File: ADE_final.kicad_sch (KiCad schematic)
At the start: 21 parts, among them J7 Conn_01x02_Pin, U8 ADE7953xCP, U9 MCP1825ST-3302E/EB, Y2 3.58M

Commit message: 2nd ADE
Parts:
- added C47, C48: 20p, Capacitor_SMD:C_0603_1608Metric, symbol Device:C
- added C49, C50, C53: 4.7u, Capacitor_SMD:C_0805_2012Metric, symbol Device:C
- added C51, C52, C54: 100n, Capacitor_SMD:C_0603_1608Metric, symbol Device:C
- added R44, R45: 10k, symbol Device:R
- added U10: ADE7953xCP, Package_CSP:LFCSP-28-1EP_5x5mm_P0.5mm_EP3.14x3.14mm, symbol Sensor:ADE7953xCP
- added Y3: 3.58M, Crystal:Crystal_SMD_HC49-SD, symbol Device:Crystal
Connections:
- net +3.3V: now also R44.2, R45.2, U10.17 (VDD), U10.7 (PULL_HIGH), U10.8 (PULL_HIGH)
- net CF1: now also U10.23 (CF1)
- net CF2: now also U10.24 (CF2)
- net GND: now also C47.2, C48.1, C49.1, C50.1, C51.1, C52.1, C53.1, C54.1, R44.1, R45.1, U10.14 (PULL_LOW), U10.16 (AGND), U10.22 (~{IRQ}), U10.28 (~{CS}), U10.29 (EP), U10.4 (DGND)
- net IBN: now also U10.10 (IBN)
- net IBP: now also U10.9 (IBP)
- net MISO: now also U10.26 (MISO/SDA/TX)
- net MOSI: now also U10.27 (MOSI/SCL/RX)
- net RESET: now also U10.2 (~{RESET})
- net REVP: now also U10.20 (~{REVP})
- net SCLK: now also U10.25 (SCLK)
- net ZX_I: now also U10.21 (ZX_I)
- net CLKIN renamed CLKIN1
- net CLKOUT renamed CLKOUT1
- net IAN renamed IAN1
- net IAP renamed IAP1
- net REF renamed REF1
- net VINTA renamed VINTA1
- net VINTD renamed VINTD1
- net VN renamed VN1
- net VP renamed VP1
- net ZX renamed ZX1
- new net CLKIN2: C47.1, U10.18 (CLKIN), Y3.1
- new net CLKOUT2: C48.2, U10.19 (CLKOUT), Y3.2
- new net IAN2: U10.6 (IAN)
- new net IAP2: U10.5 (IAP)
- new net REF2: C53.2, C54.2, U10.13 (REF)
- new net VINTA2: C50.2, C52.2, U10.15 (VINTA)
- new net VINTD2: C49.2, C51.2, U10.3 (VINTD)
- new net VN2: U10.11 (VN)
- new net VP2: U10.12 (VP)
- new net ZX2: U10.1 (ZX)
- no-connect marks 0 -> 6
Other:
- note added: "ADE CH2"
- moved on the sheet: C35, C36, C37, C38, U9, Y2

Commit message: NEW 1A LDO
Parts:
- removed U9: MCP1825ST-3302E/EB, SmartSupplyLib:DDPAK3_MC_MCH, symbol SmartSupplyLib:MCP1825ST-3302E_EB
- added IC3: MIC39100-3.3WS, SOT230P700X180-4N, symbol SamacSys_Parts:MIC39100-3.3WS
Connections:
- net +3.3V: now also IC3.3 (OUT)
- net +5V: now also IC3.1 (IN)
- net GND: now also IC3.2 (GND_1), IC3.4 (GND_2)
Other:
- moved on the sheet: C37, C38

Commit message: CHANGED RELAYS AND CONNECTORS
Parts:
- removed C37: 4.7u, Capacitor_SMD:C_0805_2012Metric, symbol Device:C
- removed C38: 10u, Capacitor_SMD:C_0805_2012Metric, symbol Device:C
- removed IC3: MIC39100-3.3WS, SOT230P700X180-4N, symbol SamacSys_Parts:MIC39100-3.3WS
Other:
- note removed: "Linear voltage regulator"

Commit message: added SD and minor fixes
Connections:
- net IBN is gone; now on net GND: U10.10 (IBN), U8.10 (IBN)
- net IBP is gone; now on net GND: U10.9 (IBP), U8.9 (IBP)
- net GND: no longer R24.1, R25.1, R44.1, R45.1, U10.22 (~{IRQ}), U10.28 (~{CS}), U8.22 (~{IRQ}), U8.28 (~{CS})
- new net CS1: R25.1, U8.28 (~{CS})
- new net CS2: R45.1, U10.28 (~{CS})
- new net IRQ1: R24.1, U8.22 (~{IRQ})
- new net IRQ2: R44.1, U10.22 (~{IRQ})
- no-connect marks 6 -> 4

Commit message: Footprint assignment
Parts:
- C30, C31, C33, C34, C35, C36, C47, C48, C51, C52, C54: footprint Capacitor_SMD:C_0603_1608Metric -> Capacitor_SMD:C_0805_2012Metric
- R24, R25, R44, R45: footprint (none) -> Resistor_SMD:R_0805_2012Metric
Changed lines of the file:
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@@
 			)
 		)
-		(property "Footprint" "Capacitor_SMD:C_0603_1608Metric"
+		(property "Footprint" "Capacitor_SMD:C_0805_2012Metric"
 			(at 132.08 33.3248 0)
 			(hide yes)
@@
 			)
 		)
-		(property "Footprint" ""
+		(property "Footprint" "Resistor_SMD:R_0805_2012Metric"
 			(at 100.838 111.76 90)
 			(hide yes)
@@
 			)
 		)
-		(property "Footprint" ""
+		(property "Footprint" "Resistor_SMD:R_0805_2012Metric"
 			(at 76.708 111.76 90)
 			(hide yes)
@@
 			)
 		)
-		(property "Footprint" "Capacitor_SMD:C_0603_1608Metric"
+		(property "Footprint" "Capacitor_SMD:C_0805_2012Metric"
 			(at 77.7748 16.51 0)
 			(hide yes)
@@
 			)
 		)
-		(property "Footprint" ""
+		(property "Footprint" "Resistor_SMD:R_0805_2012Metric"
 			(at 86.868 111.76 90)
 			(hide yes)
@@
 			)
 		)
-		(property "Footprint" "Capacitor_SMD:C_0603_1608Metric"
+		(property "Footprint" "Capacitor_SMD:C_0805_2012Metric"
 			(at 132.08 16.8148 0)
 			(hide yes)
@@
 			)
 		)
-		(property "Footprint" "Capacitor_SMD:C_0603_1608Metric"
+		(property "Footprint" "Capacitor_SMD:C_0805_2012Metric"
 			(at 32.0548 33.02 0)
 			(hide yes)
@@
 			)
 		)
-		(property "Footprint" "Capacitor_SMD:C_0603_1608Metric"
+		(property "Footprint" "Capacitor_SMD:C_0805_2012Metric"
 			(at 124.46 24.4348 0)
 			(hide yes)
@@
 			)
 		)
-		(property "Footprint" "Capacitor_SMD:C_0603_1608Metric"
+		(property "Footprint" "Capacitor_SMD:C_0805_2012Metric"
 			(at 100.6348 16.51 0)
 			(hide yes)
@@
 			)
 		)
-		(property "Footprint" ""
+		(property "Footprint" "Resistor_SMD:R_0805_2012Metric"
 			(at 110.998 111.76 90)
 			(hide yes)
@@
 			)
 		)
-		(property "Footprint" "Capacitor_SMD:C_0603_1608Metric"
+		(property "Footprint" "Capacitor_SMD:C_0805_2012Metric"
 			(at 77.7748 33.02 0)
 			(hide yes)
@@
 			)
 		)
-		(property "Footprint" "Capacitor_SMD:C_0603_1608Metric"
+		(property "Footprint" "Capacitor_SMD:C_0805_2012Metric"
 			(at 79.7052 91.44 0)
 			(hide yes)
@@
 			)
 		)
-		(property "Footprint" "Capacitor_SMD:C_0603_1608Metric"
+		(property "Footprint" "Capacitor_SMD:C_0805_2012Metric"
 			(at 124.46 40.9448 0)
 			(hide yes)
@@
 			)
 		)
-		(property "Footprint" "Capacitor_SMD:C_0603_1608Metric"
+		(property "Footprint" "Capacitor_SMD:C_0805_2012Metric"
 			(at 32.0548 16.51 0)
 			(hide yes)
@@
 			)
 		)
-		(property "Footprint" "Capacitor_SMD:C_0603_1608Metric"
+		(property "Footprint" "Capacitor_SMD:C_0805_2012Metric"
 			(at 54.9148 16.51 0)
 			(hide yes)

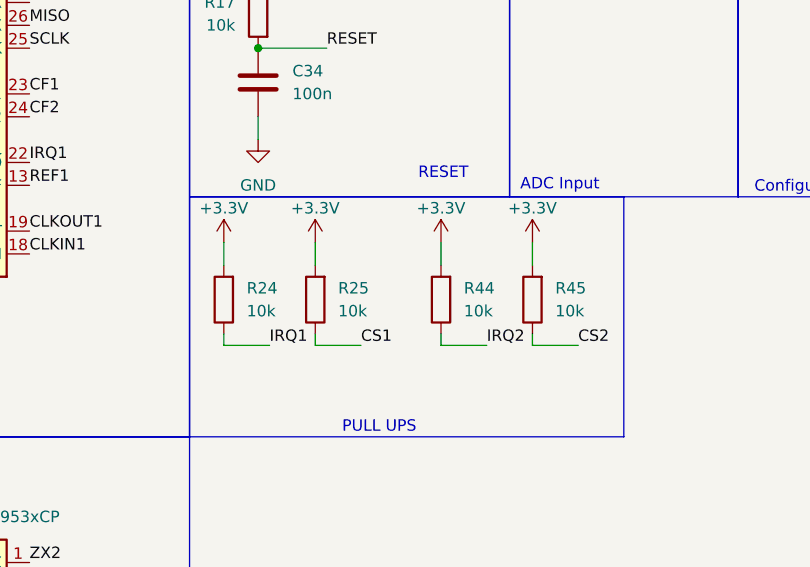
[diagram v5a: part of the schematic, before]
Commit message: add leds
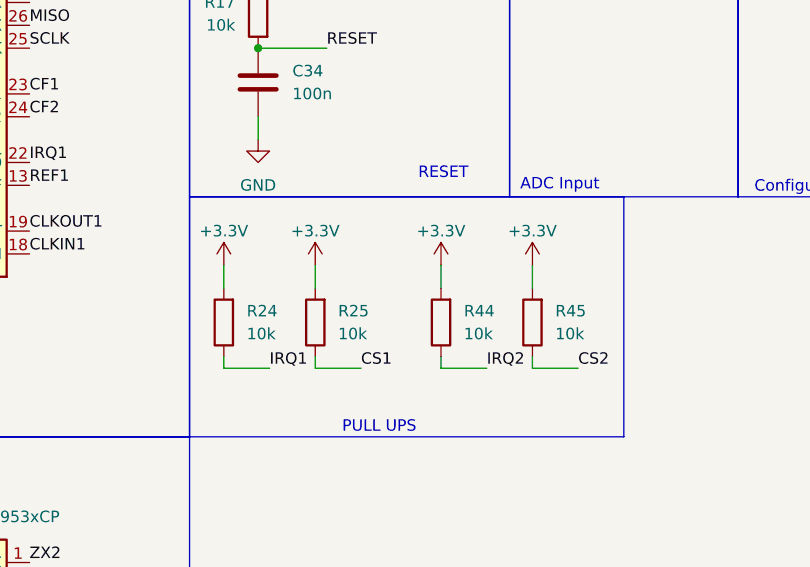
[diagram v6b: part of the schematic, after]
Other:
- moved on the sheet: R24, R25, R44, R45
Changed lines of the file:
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@@
 	(wire
 		(pts
-			(xy 85.09 105.41) (xy 85.09 107.95)
+			(xy 85.09 107.95) (xy 85.09 110.49)
 		)
 		(stroke
@@
 	(wire
 		(pts
-			(xy 99.06 105.41) (xy 99.06 107.95)
+			(xy 99.06 107.95) (xy 99.06 110.49)
 		)
 		(stroke
@@
 	(wire
 		(pts
-			(xy 85.09 115.57) (xy 85.09 116.84)
+			(xy 85.09 118.11) (xy 85.09 119.38)
 		)
 		(stroke
@@
 	(wire
 		(pts
-			(xy 109.22 105.41) (xy 109.22 107.95)
+			(xy 109.22 107.95) (xy 109.22 110.49)
 		)
 		(stroke
@@
 	(wire
 		(pts
-			(xy 74.93 105.41) (xy 74.93 107.95)
+			(xy 74.93 107.95) (xy 74.93 110.49)
 		)
 		(stroke
@@
 	(wire
 		(pts
-			(xy 99.06 115.57) (xy 99.06 116.84)
+			(xy 99.06 118.11) (xy 99.06 119.38)
 		)
 		(stroke
@@
 	(wire
 		(pts
-			(xy 85.09 116.84) (xy 90.17 116.84)
+			(xy 85.09 119.38) (xy 90.17 119.38)
 		)
 		(stroke
@@
 	(wire
 		(pts
-			(xy 74.93 115.57) (xy 74.93 116.84)
+			(xy 74.93 118.11) (xy 74.93 119.38)
 		)
 		(stroke
@@
 	(wire
 		(pts
-			(xy 109.22 115.57) (xy 109.22 116.84)
+			(xy 109.22 118.11) (xy 109.22 119.38)
 		)
 		(stroke
@@
 	(wire
 		(pts
-			(xy 74.93 116.84) (xy 80.01 116.84)
+			(xy 74.93 119.38) (xy 80.01 119.38)
 		)
 		(stroke
@@
 	(wire
 		(pts
-			(xy 109.22 116.84) (xy 114.3 116.84)
+			(xy 109.22 119.38) (xy 114.3 119.38)
 		)
 		(stroke
@@
 	(wire
 		(pts
-			(xy 99.06 116.84) (xy 104.14 116.84)
+			(xy 99.06 119.38) (xy 104.14 119.38)
 		)
 		(stroke
@@
 	)
 	(label "IRQ1"
-		(at 80.01 116.84 0)
+		(at 80.01 119.38 0)
 		(effects
 			(font
@@
 	)
 	(label "CS1"
-		(at 90.17 116.84 0)
+		(at 90.17 119.38 0)
 		(effects
 			(font
@@
 	)
 	(label "IRQ2"
-		(at 104.14 116.84 0)
+		(at 104.14 119.38 0)
 		(effects
 			(font
@@
 	)
 	(label "CS2"
-		(at 114.3 116.84 0)
+		(at 114.3 119.38 0)
 		(effects
 			(font
@@
 	(symbol
 		(lib_id "Device:R")
-		(at 99.06 111.76 180)
+		(at 99.06 114.3 180)
 		(unit 1)
 		(body_style 1)
@@
 		(fields_autoplaced yes)
 		(property "Reference" "R44"
-			(at 101.6 110.4899 0)
+			(at 101.6 113.0299 0)
 			(show_name no)
 			(do_not_autoplace no)
@@
 		)
 		(property "Value" "10k"
-			(at 101.6 113.0299 0)
+			(at 101.6 115.5699 0)
 			(show_name no)
 			(do_not_autoplace no)
@@
 		)
 		(property "Footprint" "Resistor_SMD:R_0805_2012Metric"
-			(at 100.838 111.76 90)
+			(at 100.838 114.3 90)
 			(hide yes)
 			(show_name no)
@@
 		)
 		(property "Datasheet" ""
-			(at 99.06 111.76 0)
+			(at 99.06 114.3 0)
 			(hide yes)
 			(show_name no)
@@
 		)
 		(property "Description" "Resistor"
-			(at 99.06 111.76 0)
+			(at 99.06 114.3 0)
 			(hide yes)
 			(show_name no)
@@
 	(symbol
 		(lib_id "power:+3.3V")
-		(at 99.06 105.41 0)
+		(at 99.06 107.95 0)
 		(unit 1)
 		(body_style 1)
@@
 		(dnp no)
 		(property "Reference" "#PWR098"
-			(at 99.06 109.22 0)
+			(at 99.06 111.76 0)
 			(hide yes)
 			(show_name no)
@@
 		)
 		(property "Value" "+3.3V"
-			(at 99.06 101.6 0)
+			(at 99.06 104.14 0)
 			(show_name no)
 			(do_not_autoplace no)
@@
 		)
 		(property "Footprint" "Package_DFN_QFN:Diodes_UDFN3810-9_TYPE_B"
-			(at 99.06 105.41 0)
+			(at 99.06 107.95 0)
 			(hide yes)
 			(show_name no)
@@
 		)
 		(property "Datasheet" ""
-			(at 99.06 105.41 0)
+			(at 99.06 107.95 0)
 			(hide yes)
 			(show_name no)
@@
 		)
 		(property "Description" "Power symbol creates a global label with name \"+3.3V\""
-			(at 99.06 105.41 0)
+			(at 99.06 107.95 0)
 			(hide yes)
 			(show_name no)
@@
 	(symbol
 		(lib_id "Device:R")
-		(at 74.93 111.76 180)
+		(at 74.93 114.3 180)
 		(unit 1)
 		(body_style 1)
@@
 		(fields_autoplaced yes)
 		(property "Reference" "R24"
-			(at 77.47 110.4899 0)
+			(at 77.47 113.0299 0)
 			(show_name no)
 			(do_not_autoplace no)
@@
 		)
 		(property "Value" "10k"
-			(at 77.47 113.0299 0)
+			(at 77.47 115.5699 0)
 			(show_name no)
 			(do_not_autoplace no)
@@
 		)
 		(property "Footprint" "Resistor_SMD:R_0805_2012Metric"
-			(at 76.708 111.76 90)
+			(at 76.708 114.3 90)
 			(hide yes)
 			(show_name no)
@@
 		)
 		(property "Datasheet" ""
-			(at 74.93 111.76 0)
+			(at 74.93 114.3 0)
 			(hide yes)
 			(show_name no)
@@
 		)
 		(property "Description" "Resistor"
-			(at 74.93 111.76 0)
+			(at 74.93 114.3 0)
 			(hide yes)
 			(show_name no)
@@
 	(symbol
 		(lib_id "power:+3.3V")
-		(at 85.09 105.41 0)
+		(at 85.09 107.95 0)
 		(unit 1)
 		(body_style 1)
@@
 		(dnp no)
 		(property "Reference" "#PWR085"
-			(at 85.09 109.22 0)
+			(at 85.09 111.76 0)
 			(hide yes)
 			(show_name no)
@@
 		)
 		(property "Value" "+3.3V"
-			(at 85.09 101.6 0)
+			(at 85.09 104.14 0)
 			(show_name no)
 			(do_not_autoplace no)
@@
 		)
 		(property "Footprint" "Package_DFN_QFN:Diodes_UDFN3810-9_TYPE_B"
-			(at 85.09 105.41 0)
+			(at 85.09 107.95 0)
 			(hide yes)
 			(show_name no)
@@
 		)
 		(property "Datasheet" ""
-			(at 85.09 105.41 0)
+			(at 85.09 107.95 0)
 			(hide yes)
 			(show_name no)
@@
 		)
 		(property "Description" "Power symbol creates a global label with name \"+3.3V\""
-			(at 85.09 105.41 0)
+			(at 85.09 107.95 0)
 			(hide yes)
 			(show_name no)
@@
 	(symbol
 		(lib_id "Device:R")
-		(at 85.09 111.76 180)
+		(at 85.09 114.3 180)
 		(unit 1)
 		(body_style 1)
@@
 		(fields_autoplaced yes)
 		(property "Reference" "R25"
-			(at 87.63 110.4899 0)
+			(at 87.63 113.0299 0)
 			(show_name no)
 			(do_not_autoplace no)
@@
 		)
 		(property "Value" "10k"
-			(at 87.63 113.0299 0)
+			(at 87.63 115.5699 0)
 			(show_name no)
 			(do_not_autoplace no)
@@
 		)
 		(property "Footprint" "Resistor_SMD:R_0805_2012Metric"
-			(at 86.868 111.76 90)
+			(at 86.868 114.3 90)
 			(hide yes)
 			(show_name no)
@@
 		)
 		(property "Datasheet" ""
-			(at 85.09 111.76 0)
+			(at 85.09 114.3 0)
 			(hide yes)
 			(show_name no)
@@
 		)
 		(property "Description" "Resistor"
-			(at 85.09 111.76 0)
+			(at 85.09 114.3 0)
 			(hide yes)
 			(show_name no)
@@
 	(symbol
 		(lib_id "Device:R")
-		(at 109.22 111.76 180)
+		(at 109.22 114.3 180)
 		(unit 1)
 		(body_style 1)
@@
 		(fields_autoplaced yes)
 		(property "Reference" "R45"
-			(at 111.76 110.4899 0)
+			(at 111.76 113.0299 0)
 			(show_name no)
 			(do_not_autoplace no)
@@
 		)
 		(property "Value" "10k"
-			(at 111.76 113.0299 0)
+			(at 111.76 115.5699 0)
 			(show_name no)
 			(do_not_autoplace no)
@@
 		)
 		(property "Footprint" "Resistor_SMD:R_0805_2012Metric"
-			(at 110.998 111.76 90)
+			(at 110.998 114.3 90)
 			(hide yes)
 			(show_name no)
@@
 		)
 		(property "Datasheet" ""
-			(at 109.22 111.76 0)
+			(at 109.22 114.3 0)
 			(hide yes)
 			(show_name no)
@@
 		)
 		(property "Description" "Resistor"
-			(at 109.22 111.76 0)
+			(at 109.22 114.3 0)
 			(hide yes)
 			(show_name no)
@@
 	(symbol
 		(lib_id "power:+3.3V")
-		(at 109.22 105.41 0)
+		(at 109.22 107.95 0)
 		(unit 1)
 		(body_style 1)
@@
 		(dnp no)
 		(property "Reference" "#PWR0100"
-			(at 109.22 109.22 0)
+			(at 109.22 111.76 0)
 			(hide yes)
 			(show_name no)
@@
 		)
 		(property "Value" "+3.3V"
-			(at 109.22 101.6 0)
+			(at 109.22 104.14 0)
 			(show_name no)
 			(do_not_autoplace no)
@@
 		)
 		(property "Footprint" "Package_DFN_QFN:Diodes_UDFN3810-9_TYPE_B"
-			(at 109.22 105.41 0)
+			(at 109.22 107.95 0)
 			(hide yes)
 			(show_name no)
@@
 		)
 		(property "Datasheet" ""
-			(at 109.22 105.41 0)
+			(at 109.22 107.95 0)
 			(hide yes)
 			(show_name no)
@@
 		)
 		(property "Description" "Power symbol creates a global label with name \"+3.3V\""
-			(at 109.22 105.41 0)
+			(at 109.22 107.95 0)
 			(hide yes)
 			(show_name no)
@@
 	(symbol
 		(lib_id "power:+3.3V")
-		(at 74.93 105.41 0)
+		(at 74.93 107.95 0)
 		(unit 1)
 		(body_style 1)
@@
 		(dnp no)
 		(property "Reference" "#PWR083"
-			(at 74.93 109.22 0)
+			(at 74.93 111.76 0)
 			(hide yes)
 			(show_name no)
@@
 		)
 		(property "Value" "+3.3V"
-			(at 74.93 101.6 0)
+			(at 74.93 104.14 0)
 			(show_name no)
 			(do_not_autoplace no)
@@
 		)
 		(property "Footprint" "Package_DFN_QFN:Diodes_UDFN3810-9_TYPE_B"
-			(at 74.93 105.41 0)
+			(at 74.93 107.95 0)
 			(hide yes)
 			(show_name no)
@@
 		)
 		(property "Datasheet" ""
-			(at 74.93 105.41 0)
+			(at 74.93 107.95 0)
 			(hide yes)
 			(show_name no)
@@
 		)
 		(property "Description" "Power symbol creates a global label with name \"+3.3V\""
-			(at 74.93 105.41 0)
+			(at 74.93 107.95 0)
 			(hide yes)
 			(show_name no)

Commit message: MPN BOOT BUTTON MINOR CHANGES
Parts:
- removed C52, C54: 100n, Capacitor_SMD:C_0805_2012Metric, symbol Device:C
- added C37, C38: 100n, Capacitor_SMD:C_0805_2012Metric, symbol Device:C
- C28, C29, C32, C49, C50, C53: MPN (none) -> CL21A475KAQNNNE
- C30, C31, C33, C34, C51: MPN (none) -> CC0805KRX7R9BB104
- C35, C36, C47, C48: MPN (none) -> 0805CG200J500NT
- R17, R24, R25, R44, R45: MPN (none) -> 0805W8F1002T5E
- U10, U8: MPN (none) -> ADE7953ACPZ
- Y2, Y3: MPN (none) -> C22464956
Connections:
- net GND: now also C34.1, C37.1, C38.1; no longer C34.2, C53.1
- net REF1: now also C29.2, C31.2; no longer C32.2, C33.2
- net REF2: now also C49.2, C37.2; no longer C53.2
- net RESET: now also C34.2; no longer C34.1
- net VINTA1: now also C38.2; no longer C29.2, C31.2
- net VINTA2: now also C51.2
- net VINTD2: now also C32.2, C33.2; no longer C49.2, C51.2

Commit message: FINAL SCHEMATIC
Global nets, more ESD safety, complete bom, outlets, other fixes, ERC CLEAN
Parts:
- removed D6: LED, LED_SMD:LED_0805_2012Metric, symbol Device:LED
- removed FB3: FerriteBead_Small, Inductor_SMD:L_0805_2012Metric, symbol Device:FerriteBead_Small
- removed J7: Conn_01x02_Pin, Connector_PinHeader_2.54mm:PinHeader_1x02_P2.54mm_Vertical, symbol Connector:Conn_01x02_Pin
- removed R18: 50, Resistor_SMD:R_0805_2012Metric, symbol Device:R
- added C61, C63: 10u, Capacitor_SMD:C_1206_3216Metric, symbol Device:C
- added C62, C64: 100n, Capacitor_SMD:C_0805_2012Metric, symbol Device:C
- added D19: LED, LED_SMD:LED_0805_2012Metric, symbol Device:LED
- added FB4, FB5: FerriteBead, Capacitor_SMD:C_0603_1608Metric, symbol Device:FerriteBead
- added R57: 470, Resistor_SMD:R_0805_2012Metric, symbol Device:R
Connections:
- net +3.3V: now also FB4.1, FB5.1, R57.1; no longer U10.17 (VDD), U8.17 (VDD)
- net GND: now also C53.1, C61.2, C62.1, C63.2, C64.1, D19.1 (K)
- net VINTA1: now also C53.2
- net CF1: no longer names the net of U10.23 (CF1)
- net CF1: no longer U8.23 (CF1)
- net CF2: no longer names the net of U10.24 (CF2)
- net CF2: no longer U8.24 (CF2)
- net REVP: no longer names the net of U10.20 (~{REVP})
- net REVP: no longer U8.20 (~{REVP})
- net ZX_I: no longer names the net of U10.21 (ZX_I)
- net ZX_I: no longer U8.21 (ZX_I)
- new net: D19.2 (A), R57.2
- new net VDD1: C61.1, C62.2, FB4.2, U8.17 (VDD)
- new net VDD2: C63.1, C64.2, FB5.2, U10.17 (VDD)
- no-connect marks 4 -> 8
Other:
- note added: "FILTER"
- note removed: "ADC Input"
- note removed: "Configurable Output"
- note removed: "NC"
